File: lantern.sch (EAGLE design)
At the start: 39 parts, among them T1 2N2222B, T2 2N2222B, T3 2N2222B, T4_2SC2120Y 2N2222B, T5_2SA950 2N2907, U2 HT7733A

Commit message: RevA pcb finished, first case version
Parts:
- removed T5_2SA950: 2N2907, adafruit:2N2907
- added GAIN: AYZ0202, SparkFun-Electromechanical:AYZ0202
- added R15, R16: 15K, adafruit:R-US_R0603
- added T5: 2N2907B, blinkinlabs:2N2907B
- renumbered T4_2SC2120Y to T4
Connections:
- new net N$22: GAIN.6, R16.2
- new net N$23: GAIN.3, R15.2
- net N$13: now also T5.C; no longer T5_2SA950.C
- net N$15: now also T5.E; no longer T5_2SA950.E
- net N$16: now also T5.B; no longer T5_2SA950.B
- net N$4: now also R16.1
- net N$5: now also R15.1
- net VCC: now also GAIN.2, GAIN.5
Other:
- moved on the sheet: C1, C2, C3, C4, C5, D3, D4, LED1, LED2, R1, R10, R11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

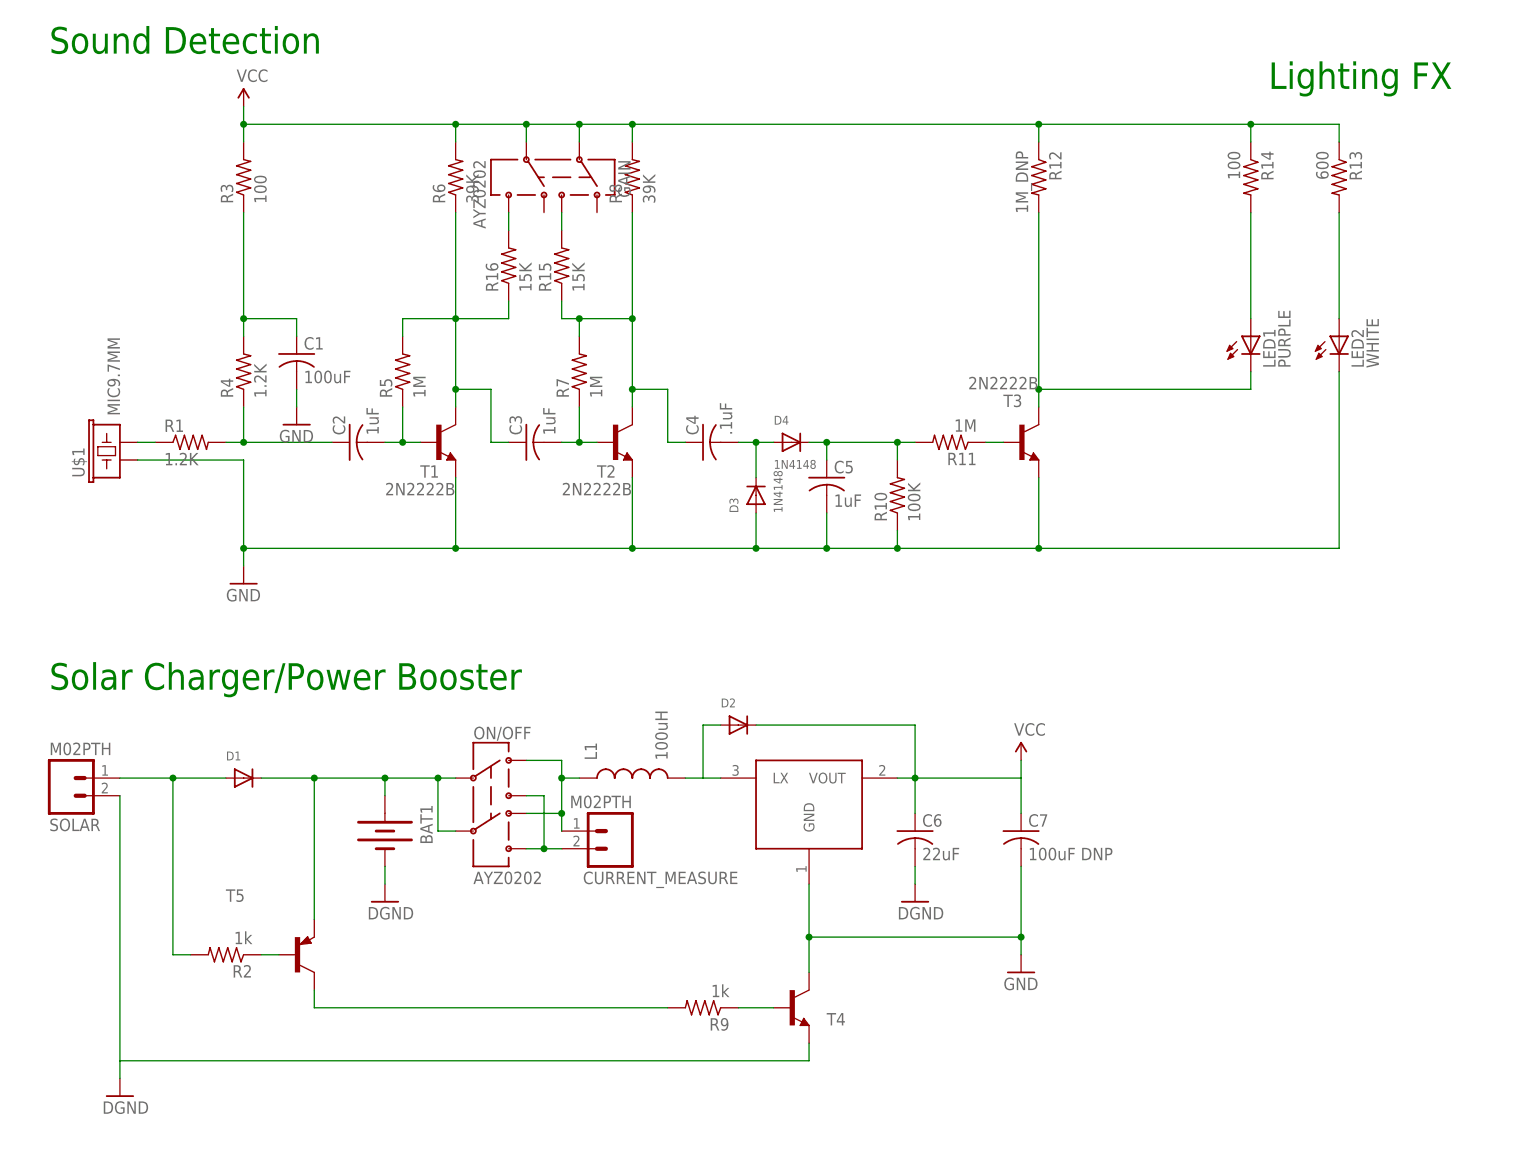
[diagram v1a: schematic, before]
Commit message: Small updates for RevB, change capacitor size and fix some labels. Hope it works!
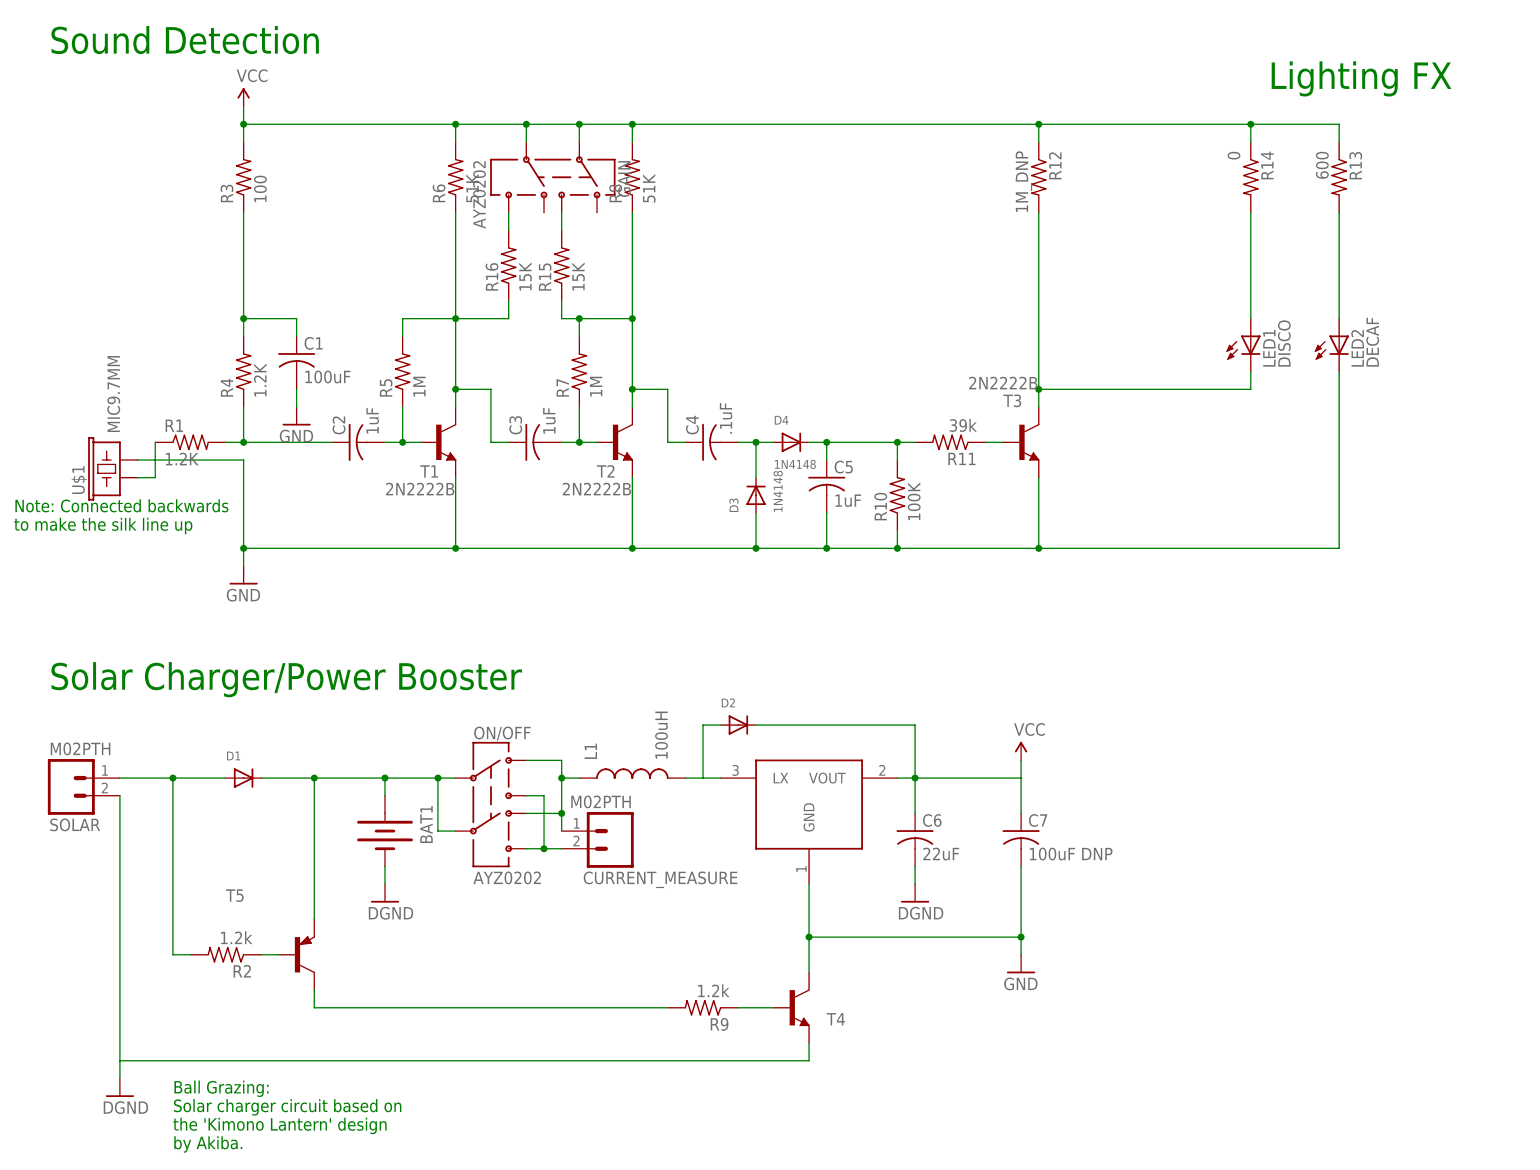
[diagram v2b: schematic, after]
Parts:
- C1, C7: device adafruit:C-USC0603 -> adafruit:C-USC1210
- LED1: value PURPLE -> DISCO
- LED2: value WHITE -> DECAF
- R11: value 1M -> 39k
- R14: value 100 -> 0
- R2, R9: value 1k -> 1.2k
- R6, R8: value 39K -> 51K
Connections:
- net GND: now also U$1.2; no longer U$1.1
- net N$7: now also U$1.1; no longer U$1.2
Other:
- note added: "Ball Grazing: Solar charger circuit based on the 'Kimono Lantern' design by Akiba."
- note added: "Note: Connected backwards to make the silk line up"
- moved on the sheet: U$1
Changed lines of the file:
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@@
 <part name="R3" library="adafruit" deviceset="R-US_" device="R0603" value="100"/>
 <part name="R5" library="adafruit" deviceset="R-US_" device="R0603" value="1M"/>
-<part name="R6" library="adafruit" deviceset="R-US_" device="R0603" value="39K"/>
+<part name="R6" library="adafruit" deviceset="R-US_" device="R0603" value="51K"/>
 <part name="R7" library="adafruit" deviceset="R-US_" device="R0603" value="1M"/>
-<part name="R8" library="adafruit" deviceset="R-US_" device="R0603" value="39K"/>
+<part name="R8" library="adafruit" deviceset="R-US_" device="R0603" value="51K"/>
 <part name="R10" library="adafruit" deviceset="R-US_" device="R0603" value="100K"/>
-<part name="R11" library="adafruit" deviceset="R-US_" device="R0603" value="1M"/>
+<part name="R11" library="adafruit" deviceset="R-US_" device="R0603" value="39k"/>
 <part name="R12" library="adafruit" deviceset="R-US_" device="R0603" value="1M_DNP"/>
-<part name="C1" library="adafruit" deviceset="C-US" device="C0603" value="100uF"/>
+<part name="C1" library="adafruit" deviceset="C-US" device="C1210" value="100uF"/>
 <part name="C2" library="adafruit" deviceset="C-US" device="C0603" value="1uF"/>
 <part name="C3" library="adafruit" deviceset="C-US" device="C0603" value="1uF"/>
@@
 <part name="BAT1" library="SparkFun-Electromechanical" deviceset="BATTERY" device="AAA"/>
 <part name="D1" library="adafruit" deviceset="DIODE" device="SOT23_REFLOW"/>
-<part name="R2" library="adafruit" deviceset="R-US_" device="R0603" value="1k"/>
-<part name="R9" library="adafruit" deviceset="R-US_" device="R0603" value="1k"/>
+<part name="R2" library="adafruit" deviceset="R-US_" device="R0603" value="1.2k"/>
+<part name="R9" library="adafruit" deviceset="R-US_" device="R0603" value="1.2k"/>
 <part name="T4" library="blinkinlabs" deviceset="2N2222" device="B"/>
 <part name="T5" library="blinkinlabs" deviceset="2N2907*" device="B"/>
@@
 <part name="GND5" library="SparkFun-Aesthetics" deviceset="DGND" device=""/>
 <part name="U$1" library="SparkFun-Sensors" deviceset="MIC" device="9.7MM"/>
-<part name="LED1" library="adafruit" deviceset="LED" device="5MM" value="PURPLE"/>
-<part name="LED2" library="adafruit" deviceset="LED" device="5MM" value="WHITE"/>
+<part name="LED1" library="adafruit" deviceset="LED" device="5MM" value="DISCO"/>
+<part name="LED2" library="adafruit" deviceset="LED" device="5MM" value="DECAF"/>
 <part name="R13" library="adafruit" deviceset="R-US_" device="R0603" value="600"/>
-<part name="R14" library="adafruit" deviceset="R-US_" device="R0603" value="100"/>
+<part name="R14" library="adafruit" deviceset="R-US_" device="R0603" value="0"/>
 <part name="CURRENT_MEASURE" library="SparkFun-Connectors" deviceset="M02" device="PTH"/>
-<part name="C7" library="adafruit" deviceset="C-US" device="C0603" value="100uF DNP"/>
+<part name="C7" library="adafruit" deviceset="C-US" device="C1210" value="100uF DNP"/>
 <part name="GAIN" library="SparkFun-Electromechanical" deviceset="AYZ0202" device=""/>
 <part name="R15" library="adafruit" deviceset="R-US_" device="R0603" value="15K"/>
@@
 <text x="10.16" y="165.1" size="3.81" layer="91">Sound Detection</text>
 <text x="185.42" y="160.02" size="3.81" layer="91">Lighting FX</text>
+<text x="27.94" y="7.62" size="1.778" layer="91">Ball Grazing:
+Solar charger circuit based on
+the 'Kimono Lantern' design
+by Akiba.</text>
+<text x="5.08" y="96.52" size="1.778" layer="91">Note: Connected backwards
+to make the silk line up</text>
 </plain>
 <instances>
@@
 <instance part="GND4" gate="G$1" x="58.42" y="43.18"/>
 <instance part="GND5" gate="G$1" x="20.32" y="15.24"/>
-<instance part="U$1" gate="G$1" x="20.32" y="106.68" rot="R90"/>
+<instance part="U$1" gate="G$1" x="20.32" y="104.14" rot="R90"/>
 <instance part="LED1" gate="G$1" x="182.88" y="124.46"/>
 <instance part="LED2" gate="G$1" x="195.58" y="124.46"/>
@@
 <junction x="121.92" y="93.98"/>
 <junction x="111.76" y="93.98"/>
-<wire x1="22.86" y1="106.68" x2="38.1" y2="106.68" width="0.1524" layer="91"/>
 <pinref part="GND2" gate="1" pin="GND"/>
-<pinref part="U$1" gate="G$1" pin="1"/>
 <pinref part="LED2" gate="G$1" pin="C"/>
 <wire x1="195.58" y1="119.38" x2="195.58" y2="93.98" width="0.1524" layer="91"/>
 <wire x1="195.58" y1="93.98" x2="152.4" y2="93.98" width="0.1524" layer="91"/>
 <junction x="152.4" y="93.98"/>
+<pinref part="U$1" gate="G$1" pin="2"/>
+<wire x1="22.86" y1="106.68" x2="38.1" y2="106.68" width="0.1524" layer="91"/>
 </segment>
 <segment>
@@
 </segment>
 </net>
-<net name="N$7" class="0">
-<segment>
-<pinref part="R1" gate="G$1" pin="1"/>
-<wire x1="25.4" y1="109.22" x2="22.86" y2="109.22" width="0.1524" layer="91"/>
-<pinref part="U$1" gate="G$1" pin="2"/>
-</segment>
-</net>
 <net name="N$13" class="0">
 <segment>
@@
 </segment>
 </net>
+<net name="N$7" class="0">
+<segment>
+<pinref part="R1" gate="G$1" pin="1"/>
+<wire x1="25.4" y1="109.22" x2="25.4" y2="104.14" width="0.1524" layer="91"/>
+<pinref part="U$1" gate="G$1" pin="1"/>
+<wire x1="25.4" y1="104.14" x2="22.86" y2="104.14" width="0.1524" layer="91"/>
+</segment>
+</net>
 </nets>
 </sheet>
@@
 </schematic>
 </drawing>
+<compatibility>
+<note version="6.3" minversion="6.2.2" severity="warning">
+Since Version 6.2.2 text objects can contain more than one line,
+which will not be processed correctly with this version.
+</note>
+</compatibility>
 </eagle>
